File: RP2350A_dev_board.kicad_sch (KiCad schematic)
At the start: 35 parts, among them J1 USB_C_Female_USB2.0_16P, SW1 Button, U1 RP2350A, U2 W25Q128JVS, U3 USBLC6-2SC6, U4 SPX3819M5-L-3-3, Y1 12MHz Crystal GND2,4

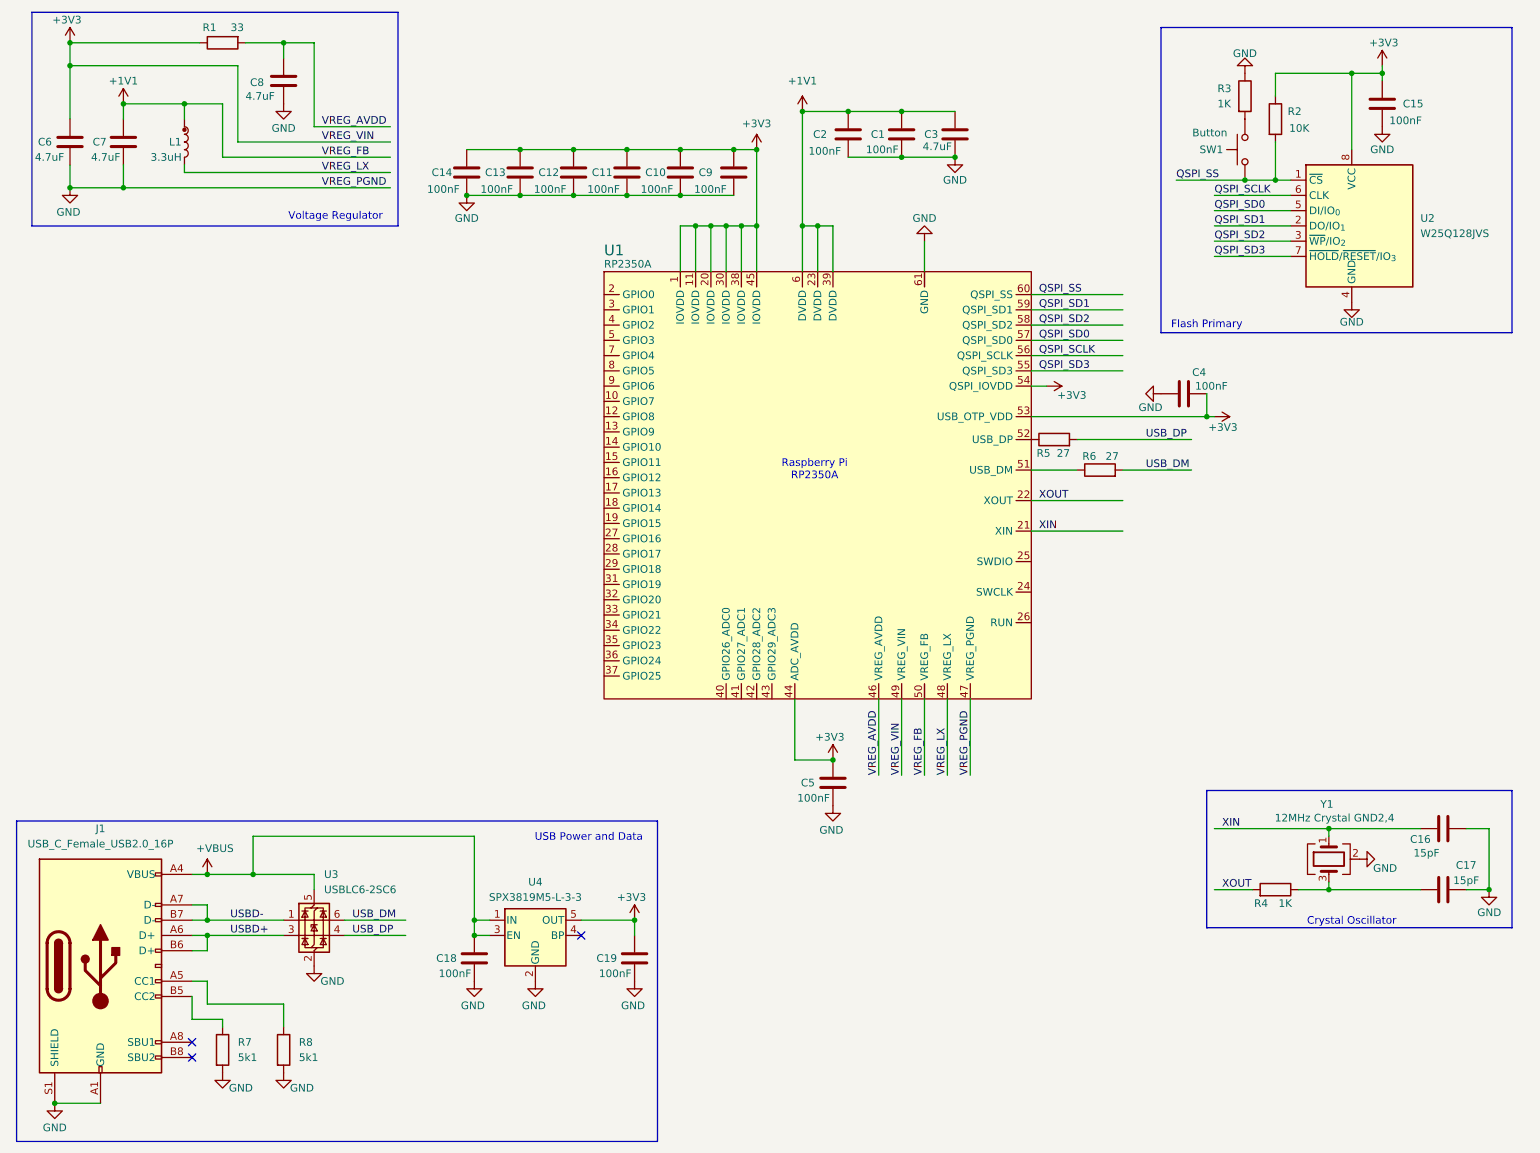
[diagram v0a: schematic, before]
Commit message: Added Red LED, Wht LED modules. Houskeeping.
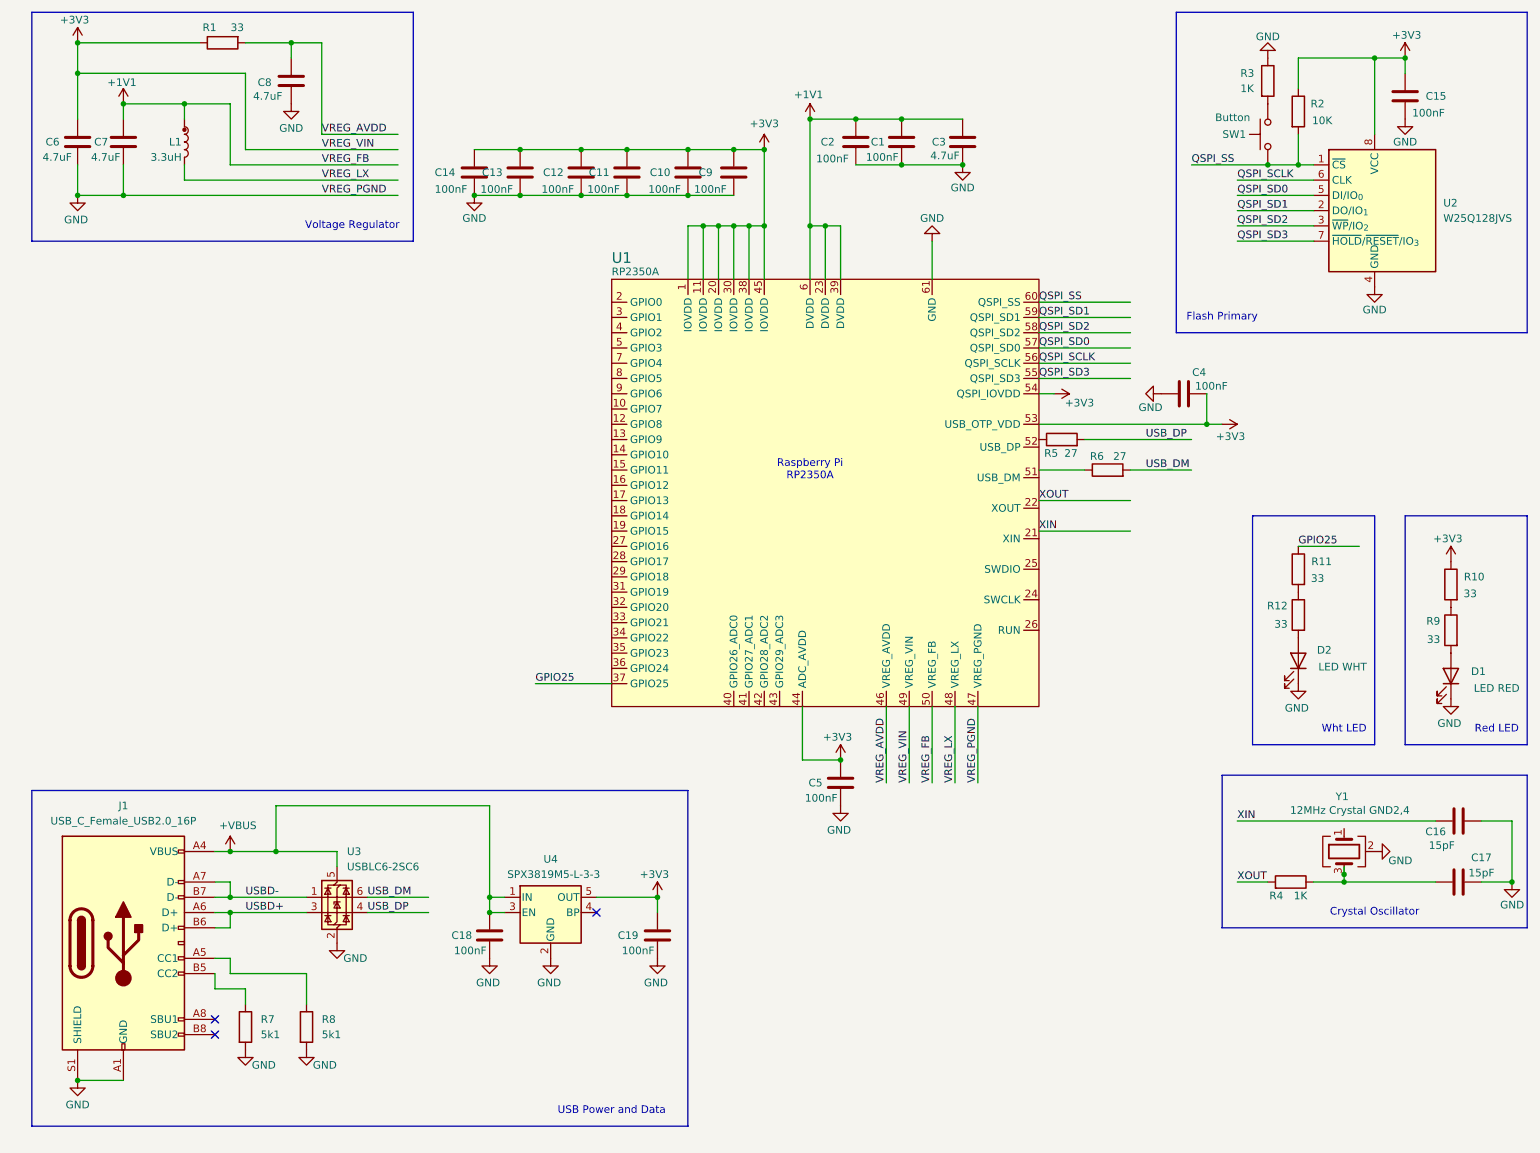
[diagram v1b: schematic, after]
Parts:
- added D1: LED RED, LED_SMD:LED_0603_1608Metric, symbol Device:LED
- added D2: LED WHT, LED_SMD:LED_0603_1608Metric, symbol Device:LED
- added R10, R11, R12, R9: 33, Resistor_SMD:R_0603_1608Metric, symbol Device:R
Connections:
- net +3V3: now also R10.1
- net GND: now also D1.1 (K), D2.1 (K)
- net XIN: no longer U1.21 (XIN), Y1.1
- net XOUT: no longer U1.22 (XOUT)
- net GPIO25: now reaches U1.37 (GPIO25)
- net GPIO25: now also R11.1
- net at U1.51 (USB_DM): no longer R6.1
- net at U1.52 (USB_DP): no longer R5.1
- new net: D1.2 (A), R9.2
- new net: D2.2 (A), R12.2
- new net: R10.2, R9.1
- new net: R11.2, R12.1
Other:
- note added: "Red LED"
- note added: "Wht LED"
- moved on the sheet: C1, C10, C12, C14, C15, C16, C17, C18, C19, C2, C3, C5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

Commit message: Added I2C Interface, Debug Interface.
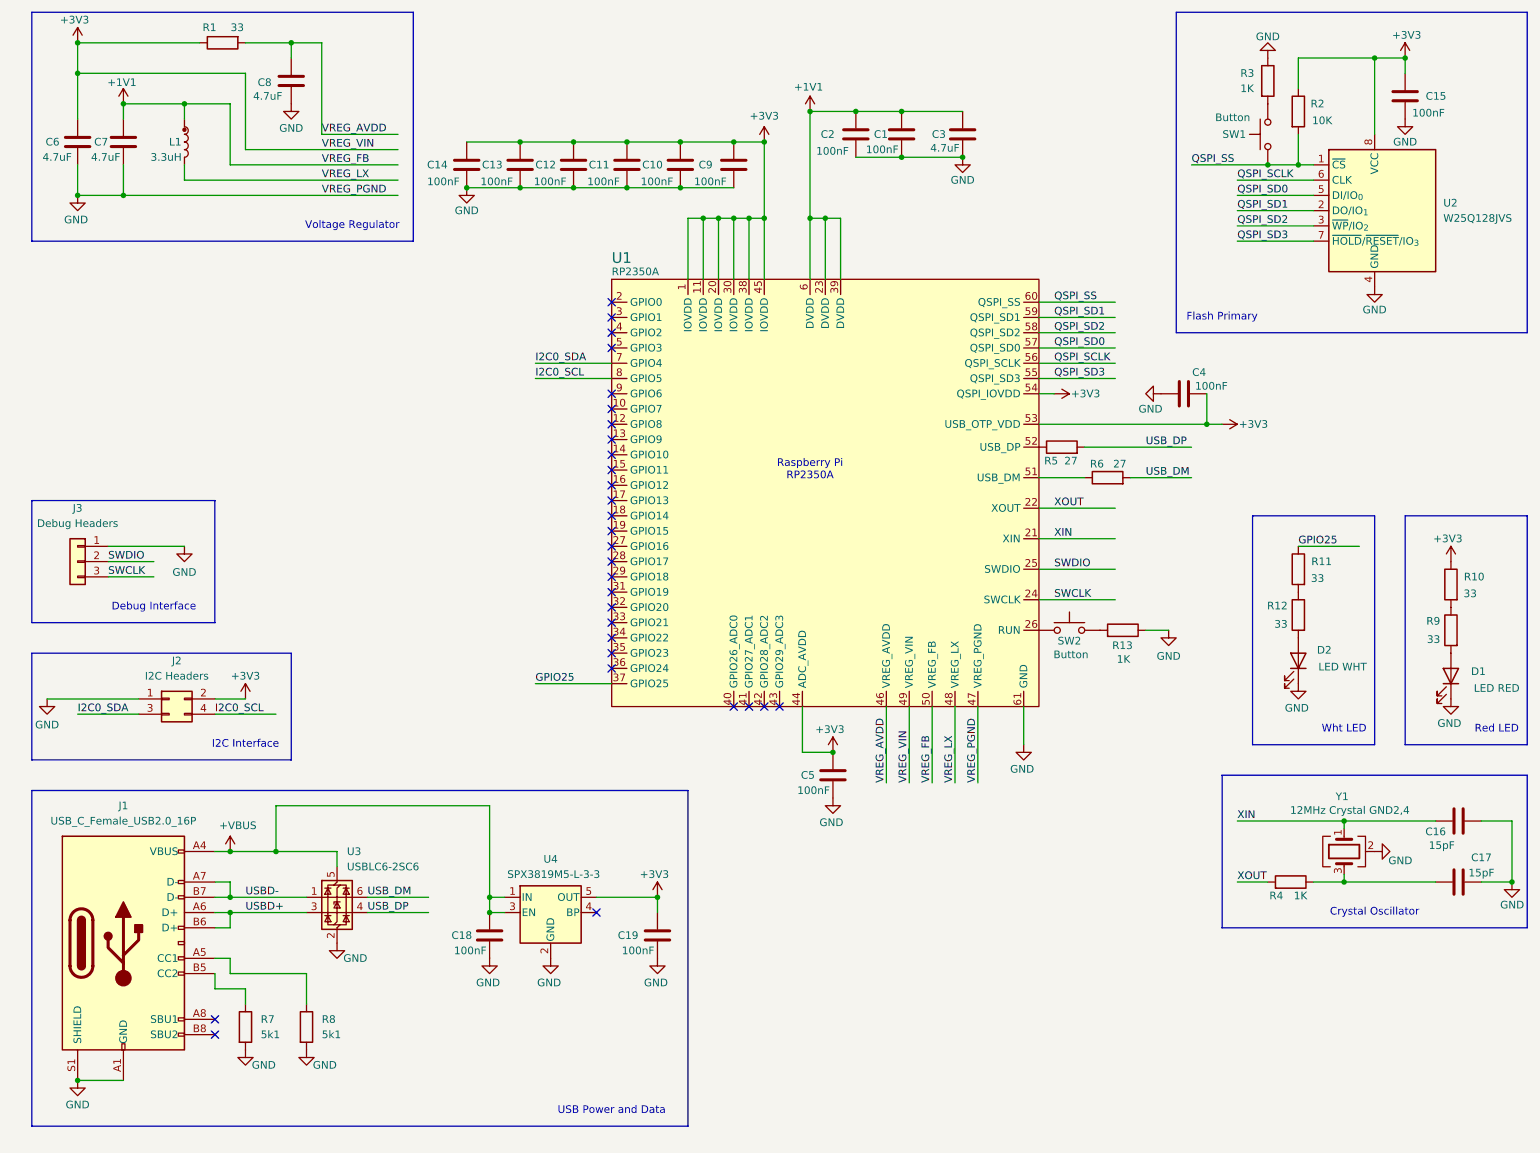
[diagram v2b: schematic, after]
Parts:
- added J2: I2C Headers, Connector_PinHeader_2.54mm:PinHeader_2x02_P2.54mm_Vertical, symbol Connector_Generic:Conn_02x02_Odd_Even
- added J3: Debug Headers, Connector_PinHeader_2.54mm:PinHeader_1x03_P2.54mm_Vertical, symbol Connector_Generic:Conn_01x03
- added R13: 1K, Resistor_SMD:R_0603_1608Metric, symbol Device:R
- added SW2: Button, Button_Switch_SMD:SW_SPST_TS-1088-xR020, symbol Switch:SW_Push
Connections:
- net +3V3: now also J2.2 (Pin_2)
- net GND: now also J2.1 (Pin_1), J3.1 (Pin_1), R13.1
- net XIN: now also U1.21 (XIN), Y1.1
- net XOUT: now also U1.22 (XOUT)
- net SWCLK: now reaches U1.24 (SWCLK)
- net SWCLK: now also J3.3 (Pin_3)
- net SWDIO: now reaches U1.25 (SWDIO)
- net SWDIO: now also J3.2 (Pin_2)
- net at U1.26 (RUN): now also SW2.1
- net at U1.51 (USB_DM): now also R6.1
- net at U1.52 (USB_DP): now also R5.1
- net I2C0_SDA: now reaches U1.7 (GPIO4)
- net I2C0_SDA: now also J2.3 (Pin_3)
- net I2C0_SCL: now reaches U1.8 (GPIO5)
- net I2C0_SCL: now also J2.4 (Pin_4)
- new net: R13.2, SW2.2
- no-connect marks 3 -> 30
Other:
- note added: "Debug Interface"
- note added: "I2C Interface"
- moved on the sheet: C1, C10, C11, C12, C13, C14, C2, C3, C5, C9, R5, R6

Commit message: Added and configured additional net classes. Began ERC fixes.
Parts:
- renumbered C6 to C1, C9 to C11, C5 to C12, C2 to C13, C1 to C14, C3 to C15, C4 to C16, C15 to C17, C16 to C18, C17 to C19, C7 to C2, C8 to C3, C14 to C4, C18 to C5, C13 to C6, C12 to C7, C11 to C8, C19 to C9, D2 to D1, D1 to D2, J3 to J1, J1 to J2, J2 to J3, R11 to R10, R12 to R11, R10 to R12, R9 to R13, R7 to R2, R8 to R3, R5 to R4, R6 to R5, R13 to R6, R3 to R7, R4 to R8, R2 to R9, SW2 to SW1, SW1 to SW2, U3 to U1, U4 to U2, U1 to U3, U2 to U4
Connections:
- net +1V1: now also L1.2; no longer L1.
- net VREG_LX: now also L1.1; no longer L1.

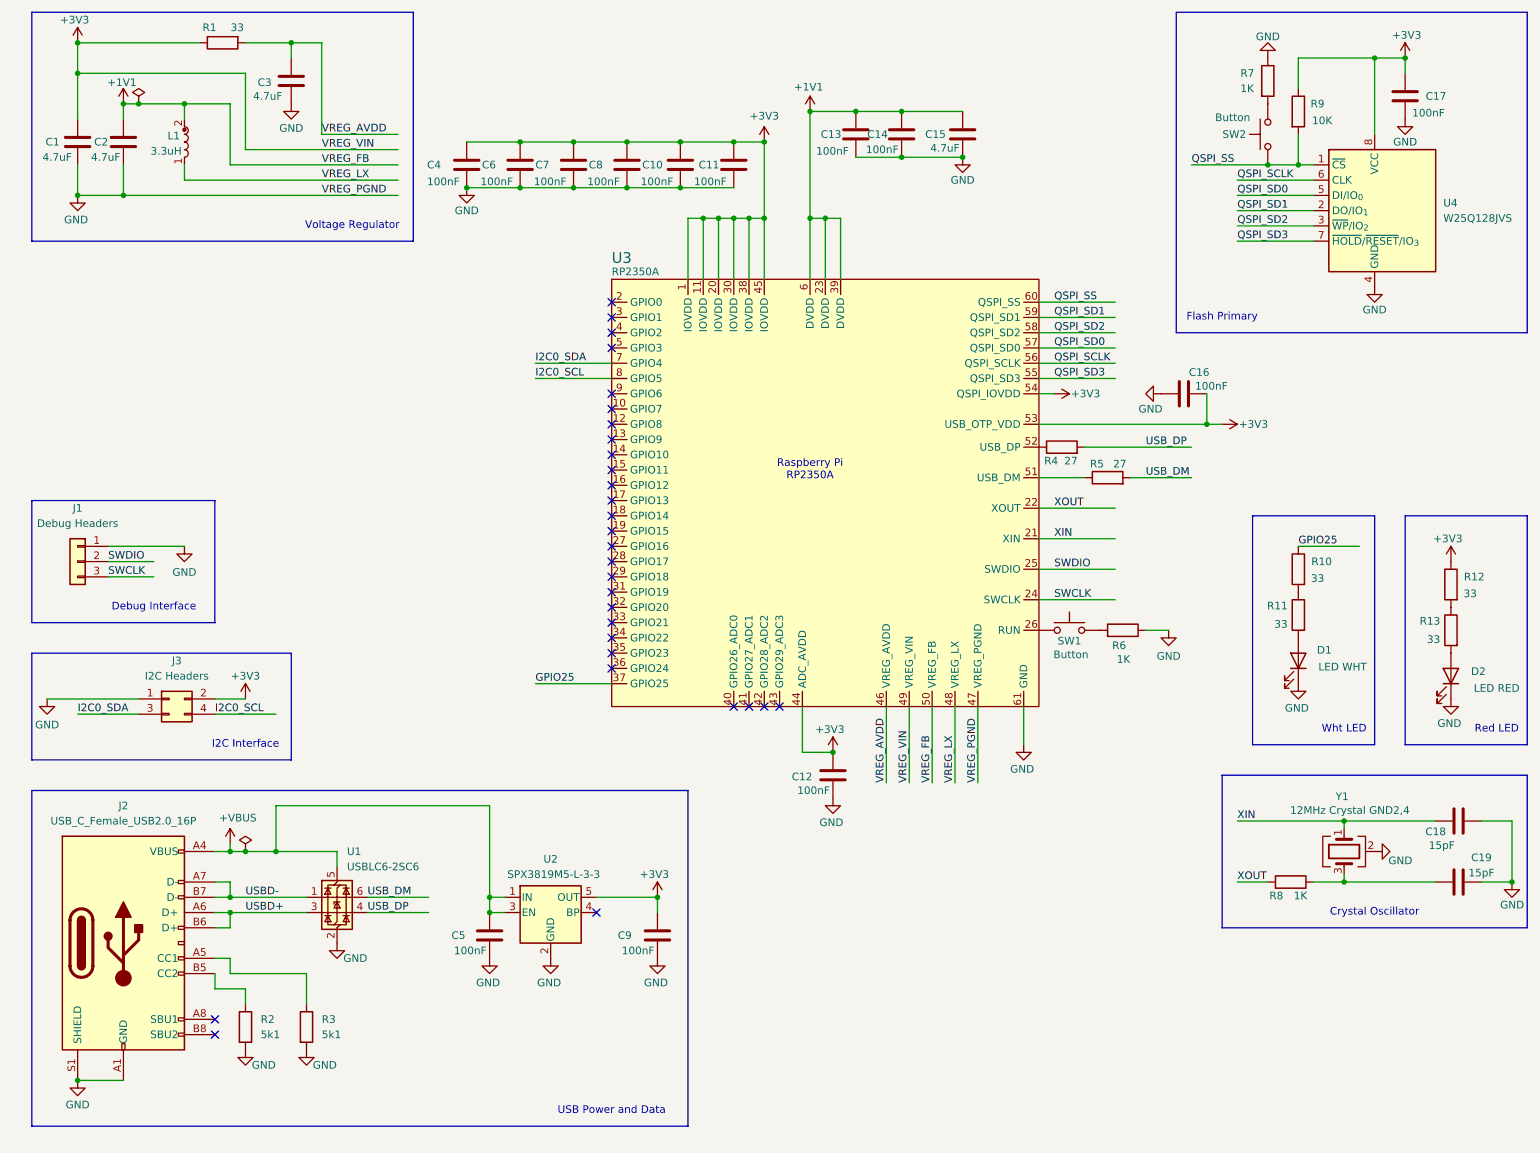
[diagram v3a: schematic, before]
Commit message: Fixed all ERC issues.
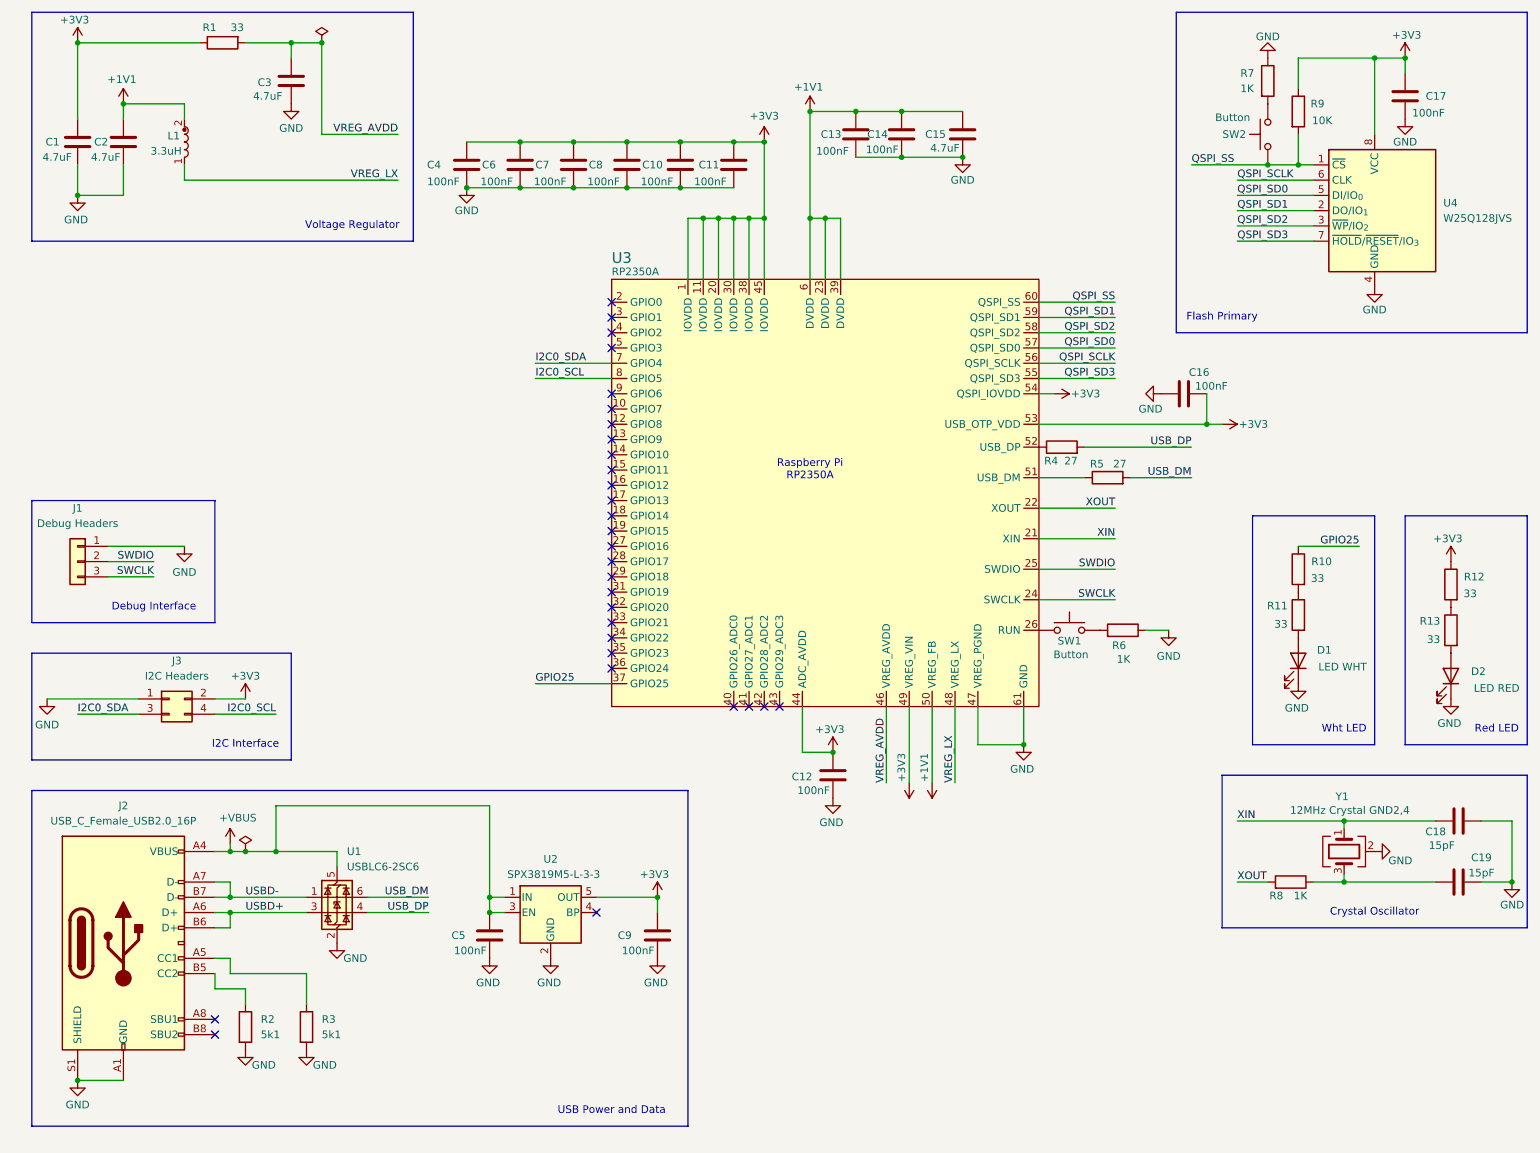
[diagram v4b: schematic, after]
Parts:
- J2: symbol Connector:USB_C_Receptacle_USB2.0_16P -> custom:USB_C_Receptacle_USB2.0_16P_custom
- L1: symbol inductor_polarised:l_polarised -> custom:OTA-B201610S3R3-101-T_custom
- U3: symbol RP2350-custom:RP2350A -> custom:RP2350A
